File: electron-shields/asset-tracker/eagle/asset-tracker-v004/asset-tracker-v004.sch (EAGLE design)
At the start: 30 parts, among them J1 1X2-3.5MM, T1 DMG3415, U1 MAX-M8, U2 MAX2674, U3 LIS3DHTR, X1 ELECTRON, X2 IPEX-20279-001E

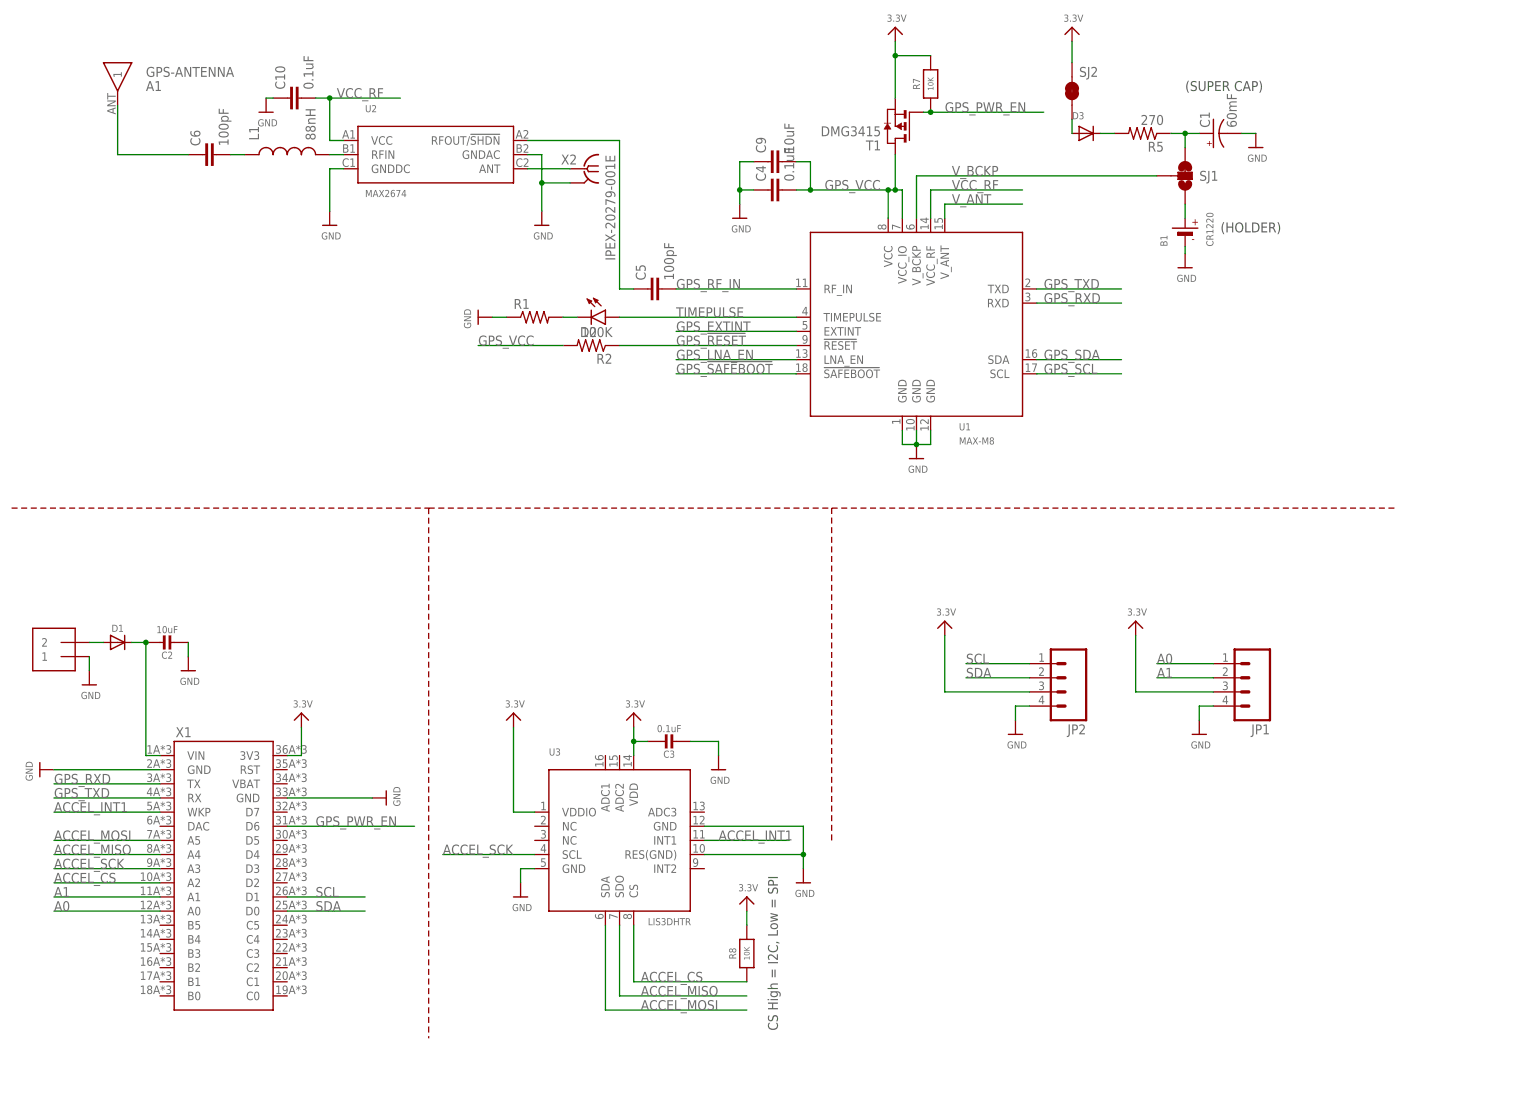
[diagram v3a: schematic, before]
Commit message: added saw filter, li ion cell and routing almost complete
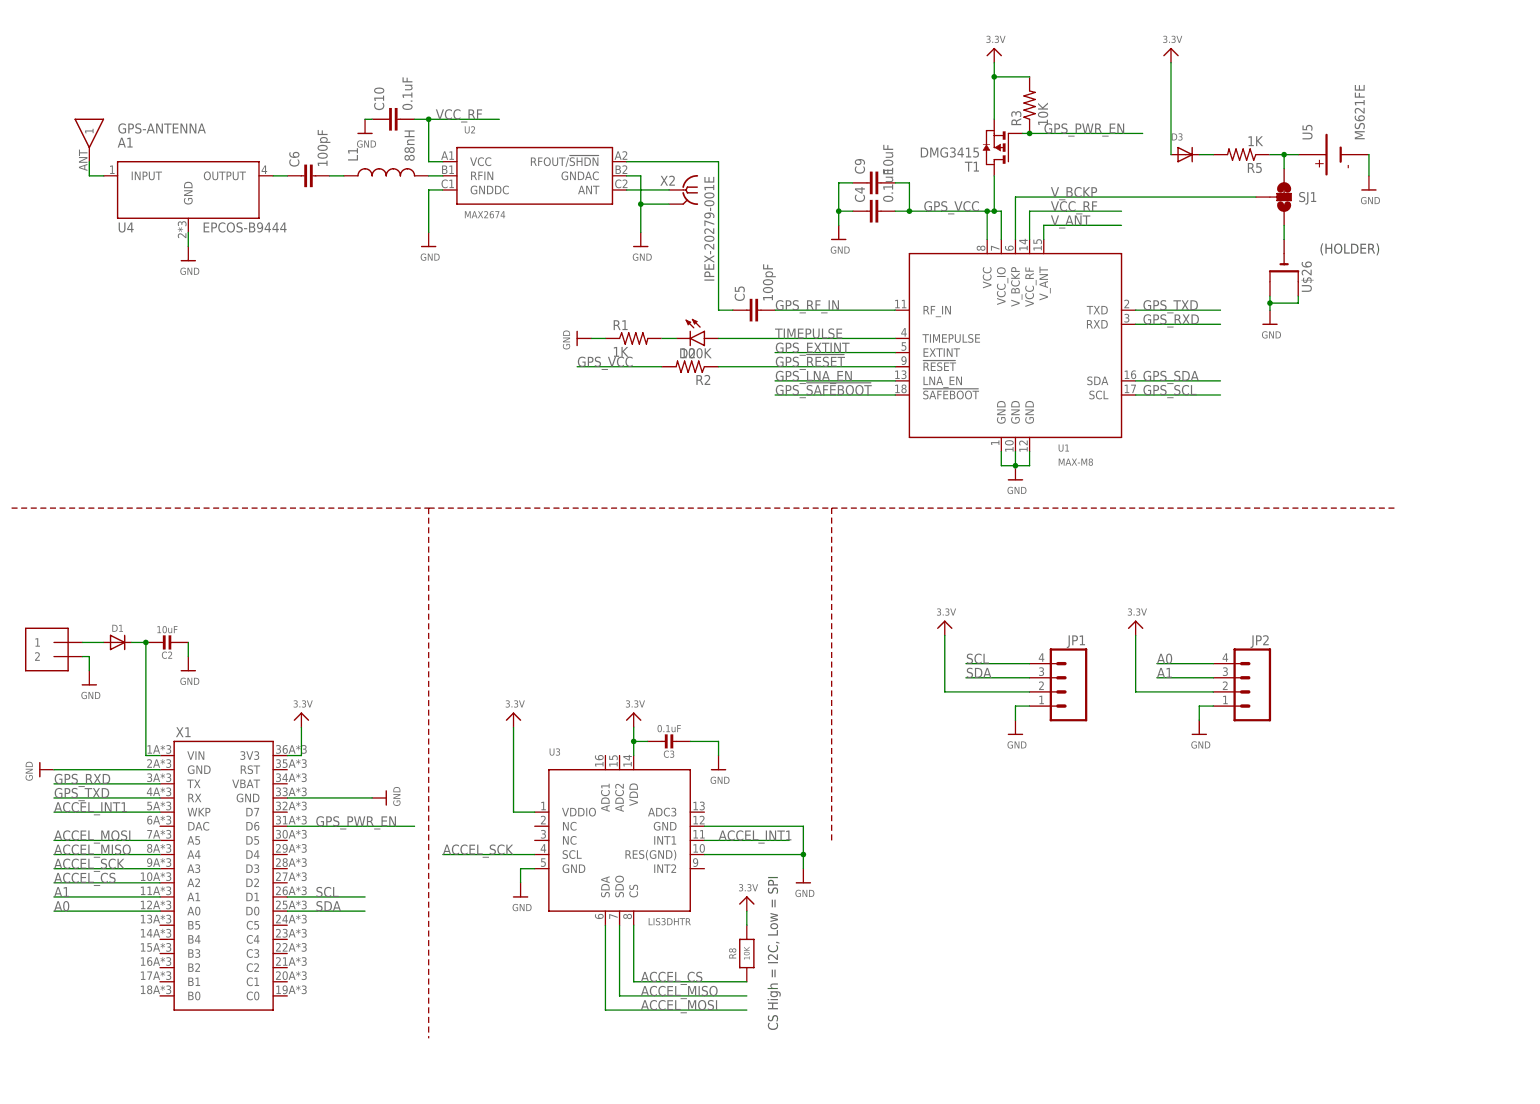
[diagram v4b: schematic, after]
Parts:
- removed B1: CR1220, microbuilder:BATTERYCR1220_SMT
- removed C1: 60mF, adafruit:SUPERCAP
- removed R7: 10K, microbuilder:RESISTOR0805_NOOUTLINE
- removed SJ2: JUMPER-PAD-2-NC_BY_TRACENO_SILK, SparkFun-Passives:JUMPER-PAD-2-NC_BY_TRACENO_SILK
- added R3: 10K, rcl:R-US_R0402
- added U$26: (no value), adafruit:CR2032SMT
- added U4: EPCOS-B9444, filters:EPCOS-B9444
- added U5: MS621FE, Explore Labs EAGLE Library:MS621FE
- C2: device microbuilder:CAP_CERAMIC0805-NOOUTLINE -> microbuilder:CAP_CERAMIC_0402MP
- C3: device microbuilder:CAP_CERAMIC0805_10MGAP -> microbuilder:CAP_CERAMIC_0402MP
- C9: device rcl:C-EUC0603K -> rcl:C-EUC0402
- JP1, JP2: device SparkFun-Connectors:M041X04_NO_SILK -> SparkFun-Connectors:M04JST-PTH-VERT
- R1: value (none) -> 1K
- R5: value 270 -> 1K; device rcl:R-US_R0603 -> rcl:R-US_R0402
- R8: device microbuilder:RESISTOR0805_NOOUTLINE -> microbuilder:RESISTOR_0402MP
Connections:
- net 3.3V: now also D3.A, JP1.2, JP2.2, R3.2; no longer JP1.3, JP2.3, R7.2, SJ2.2
- net A0: now also JP2.4; no longer JP1.1
- net A1: now also JP2.3; no longer JP1.2
- net GND: now also J1.2, JP1.1, JP2.1, U$26.+, U$26.+1, U4.GND, U5.NEG; no longer B1.-, C1.-, J1.1, JP1.4, JP2.4
- net GPS_PWR_EN: now also R3.1; no longer R7.1
- net N$1: now also C6.1, U4.OUTPUT; no longer D3.A, SJ2.1
- net N$11: now also U$26.-; no longer B1.+
- net N$12: now also U4.INPUT; no longer C6.1
- net N$7: now also U5.POS; no longer C1.+
- net N$9: now also J1.1; no longer J1.2
- net SCL: now also JP1.4; no longer JP2.1
- net SDA: now also JP1.3; no longer JP2.2
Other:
- note removed: "(SUPER CAP)"
- moved on the sheet: A1, C10, C4, C5, C6, C9, D2, D3, JP1, JP2, L1, R1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
